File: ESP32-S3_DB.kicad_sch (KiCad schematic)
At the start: 0 parts

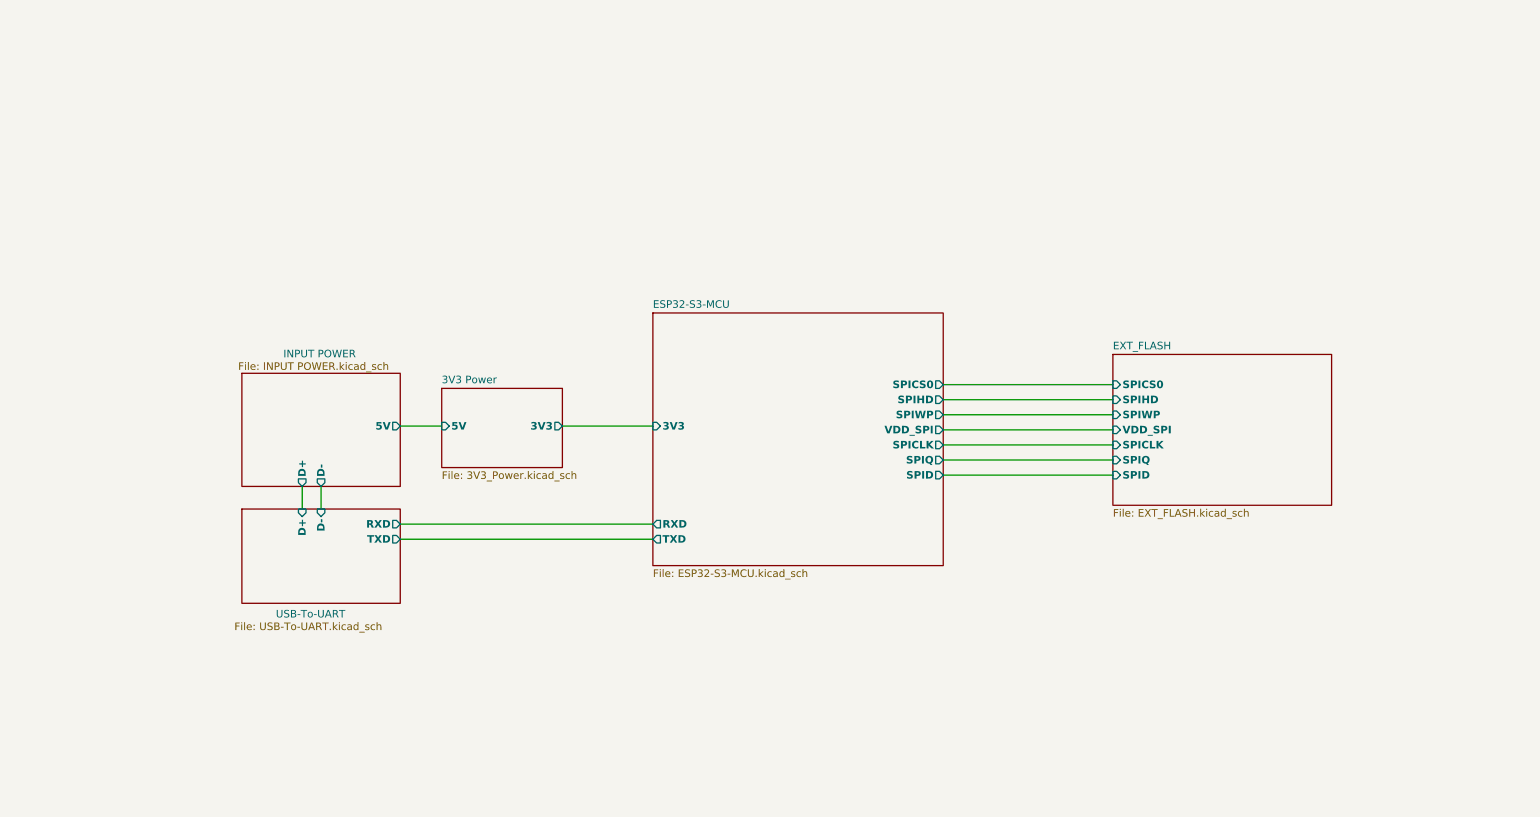
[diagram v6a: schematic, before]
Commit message: Added RS-485 Transceiver
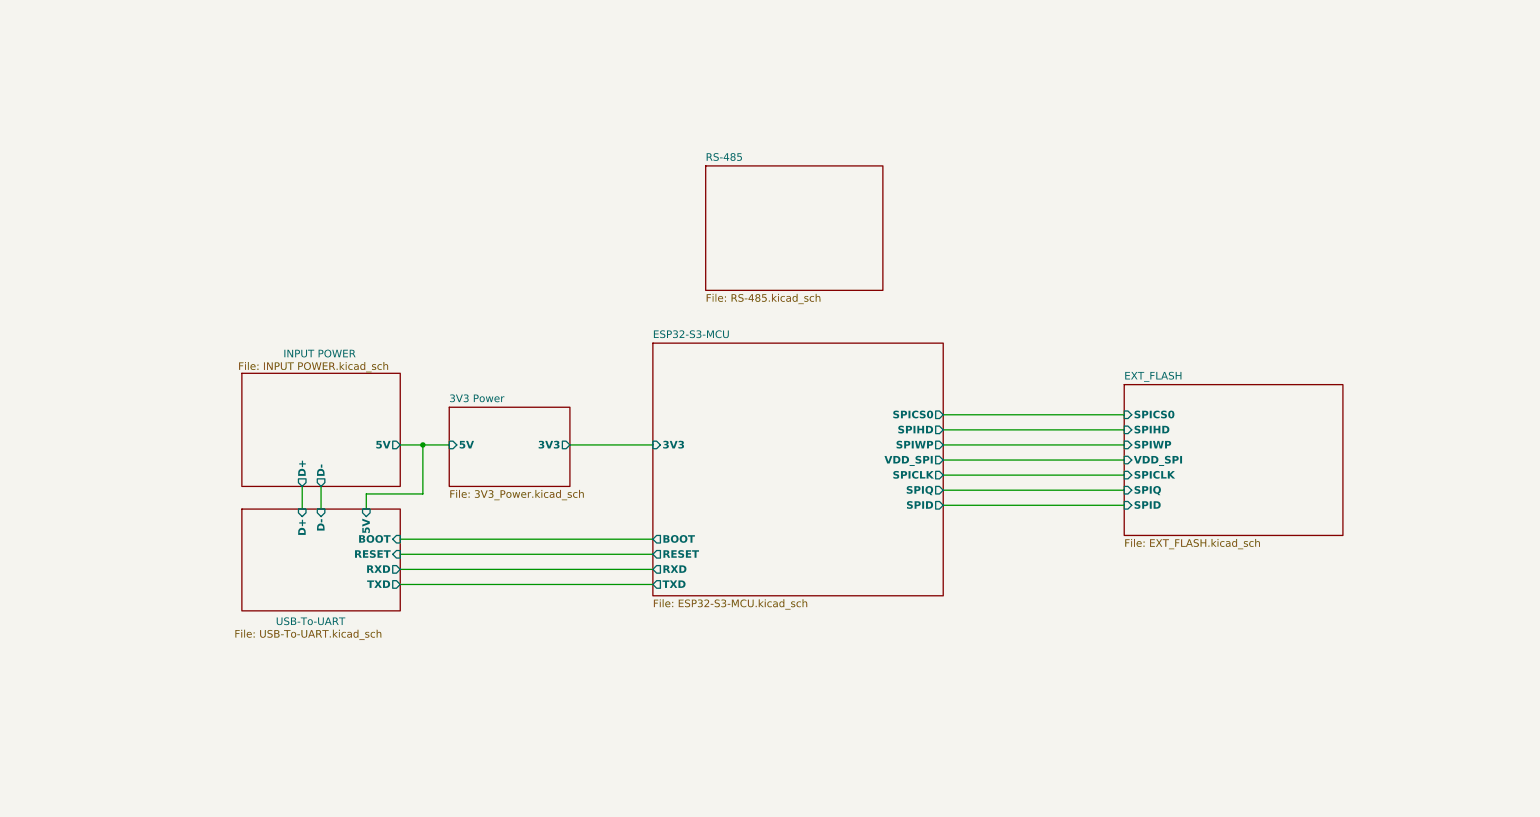
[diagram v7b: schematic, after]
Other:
- added sheet RS-485 (RS-485.kicad_sch)
- sheet ESP32-S3-MCU ports: added BOOT, RESET; removed none
- sheet USB-To-UART ports: added 5V, BOOT, RESET; removed none

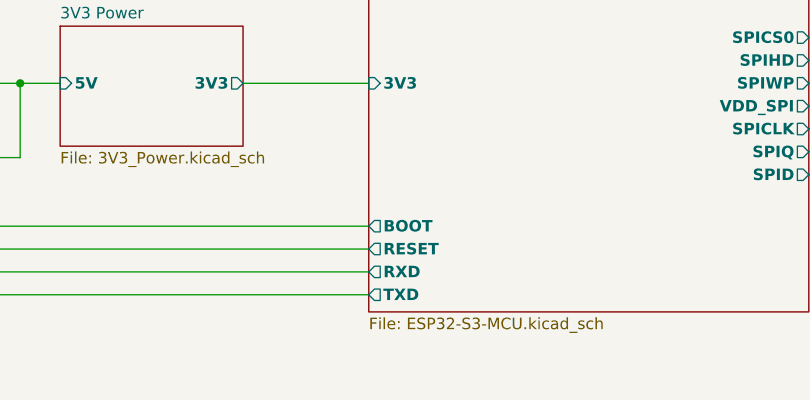
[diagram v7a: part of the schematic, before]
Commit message: UART Tx and Rx correctly placed
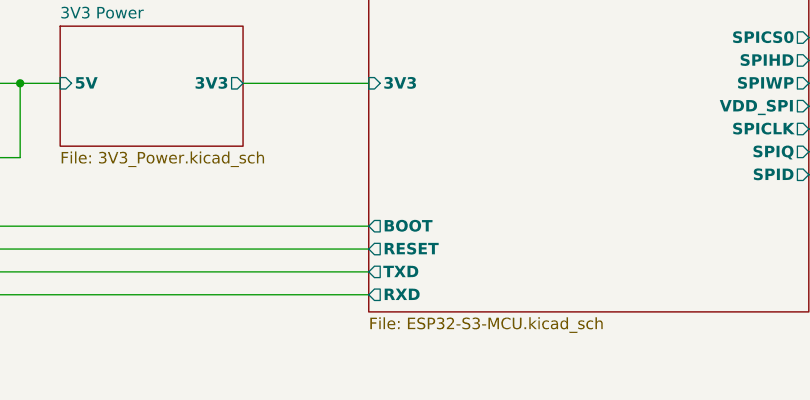
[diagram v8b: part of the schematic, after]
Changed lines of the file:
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@@
       (effects (font (size 1.27 1.27) (thickness 0.254) bold (color 0 0 255 1)) (justify right))
     )
-    (pin "TXD" output (at 125.095 115.57 180)
+    (pin "TXD" output (at 125.095 113.03 180)
       (effects (font (size 1.27 1.27) (thickness 0.254) bold (color 0 0 255 1)) (justify left))
     )
-    (pin "RXD" output (at 125.095 113.03 180)
+    (pin "RXD" output (at 125.095 115.57 180)
       (effects (font (size 1.27 1.27) (thickness 0.254) bold (color 0 0 255 1)) (justify left))
     )
